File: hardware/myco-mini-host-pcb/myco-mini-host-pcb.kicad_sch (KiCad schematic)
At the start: 22 parts, among them J1 Conn_01x17_Female, J2 Conn_01x17_Female, Q1 AO3401A, Q2 AO3401A, SW1 EM-04-Q, U1 XC9145B33C0R-G, U2 SHT40-AD1B-R2, U3 BH1750FVI-TR

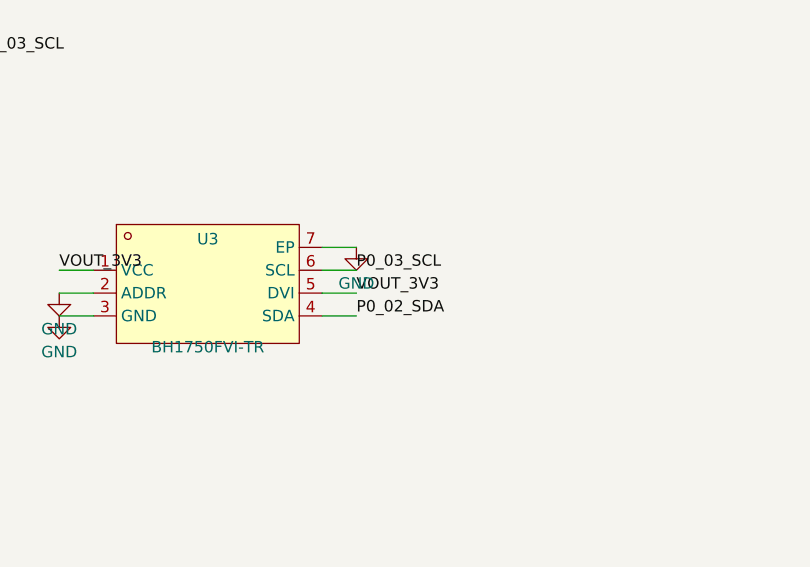
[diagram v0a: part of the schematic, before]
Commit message: fix: DVI du BH1750 sur VDD_NRF au lieu de VOUT_3V3 (cohérence avec les pull-ups I2C)
Le datasheet ROHM BH1750FVI définit VIH1 = 0.7 x DVI comme seuil logique haut
sur SDA/SCL. DVI était câblée sur VOUT_3V3 (3.3V fixe) alors que les pull-ups
I2C (R1/R2) sont sur VDD_NRF (~3.0V CR2032, peut descendre vers ~2.0V en fin
de vie de pile) — le seuil (2.31V) pouvait dépasser la tension réelle du bus
en fin de vie de pile, empêchant le BH1750 de reconnaître un "haut" valide.
DVI câblée maintenant sur le même rail que les pull-ups pour que le seuil
suive la tension réelle du bus. Point de séquencement DVI/VCC résiduel
documenté dans docs/pcb-design-decisions.md (non tranché, à valider en test).

Co-Authored-By: Claude Sonnet 5 <noreply@anthropic.com>
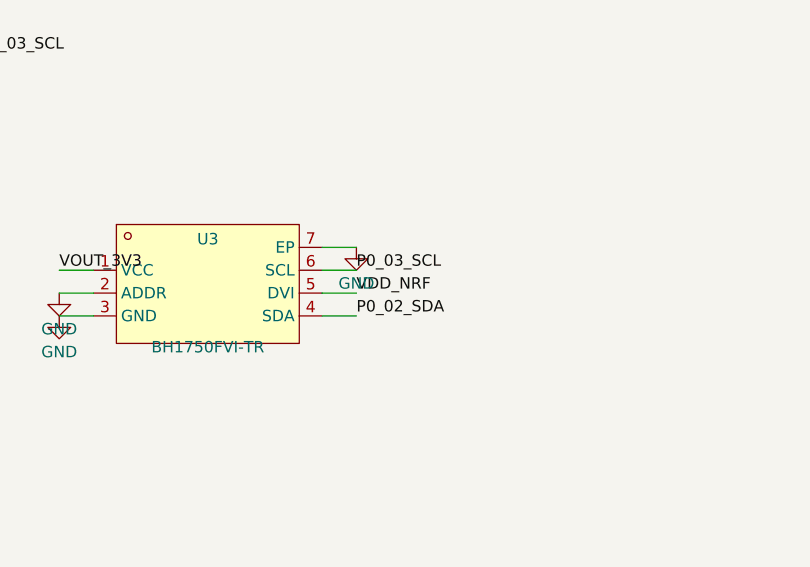
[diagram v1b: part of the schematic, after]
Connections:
- net VDD_NRF: now also U3.5 (DVI)
- net VOUT_3V3: no longer U3.5 (DVI)
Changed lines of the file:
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@@
     (effects (font (size 1.27 1.27)) (justify left bottom))
   )
-  (label "VOUT_3V3"
+  (label "VDD_NRF"
     (at 191.77 134.62 0)
     (effects (font (size 1.27 1.27)) (justify left bottom))

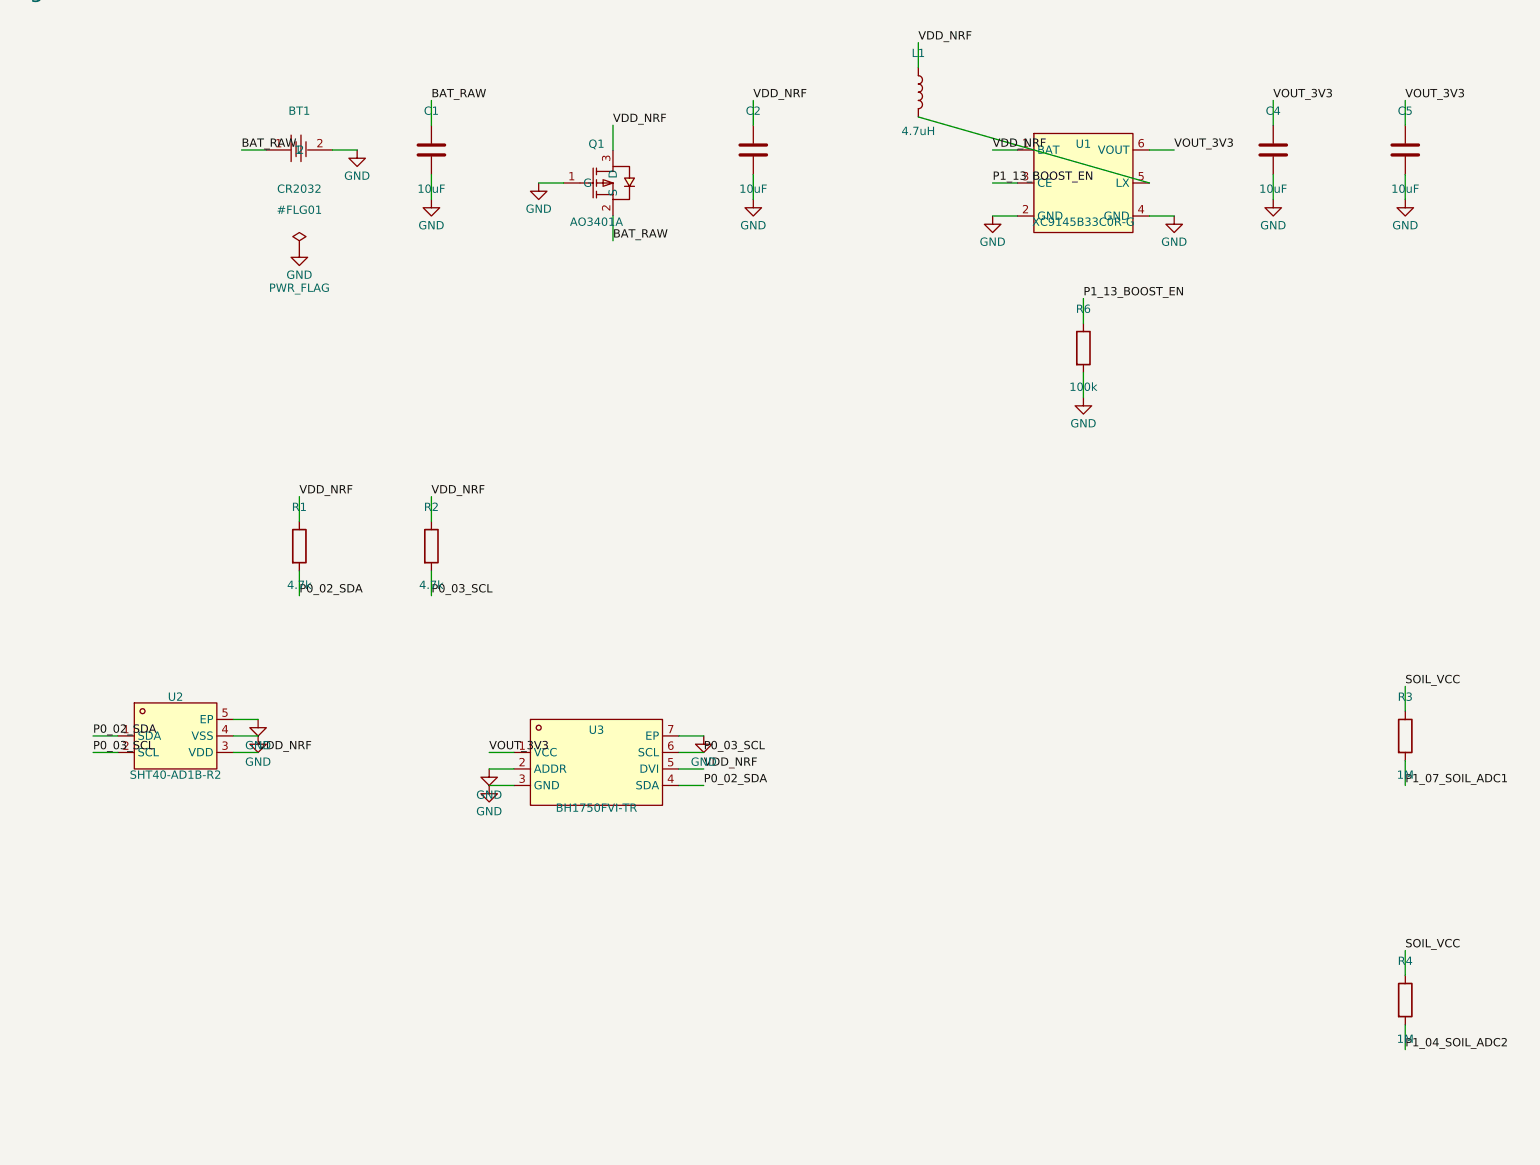
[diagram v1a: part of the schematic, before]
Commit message: fix: resolution XC9145 SOT-25, refonte sonde sol (profondeur), R3/R4 220k
- U1: XC9145B33C0R-G (WLP-6-05, non soudable a la main) -> XC9145B33CMR-G
  (SOT-25, LCSC C19261414, confirme en stock) - symbole/footprint refaits
- U2: SHT40 -> SHT41-AD1B-R2 (meme boitier/pinout, meilleure precision RH
  aux extremes)
- R3/R4: 1M -> 220k (1M hors plage source resistance max du SAADC nRF54L15,
  cf datasheet sec 11.17)
- Sonde sol: 36mm -> 60mm, doigts tournes a 90 (spines gauche/droite au
  lieu de haut/bas, moins fragiles mecaniquement), pitch 0.45mm -> 1.5mm
  et largeur 10mm -> 18mm pour la profondeur de penetration du champ dans
  le sol (~0.3mm -> ~1mm), compense par plus de doigts pour garder la
  capacite
- gen_pcb.py: PLACEMENT capture depuis le placement manuel valide (lecture
  seule du board actuel, pas de regeneration destructive)
- docs/pcb-design-decisions.md: sections 2.6/2.7/2.9/3.2 mises a jour avec
  le detail des calculs et sources
- misc/: ajout datasheet WLP-6-05 et reference Torex SOT-25 eval board

Co-Authored-By: Claude Sonnet 5 <noreply@anthropic.com>
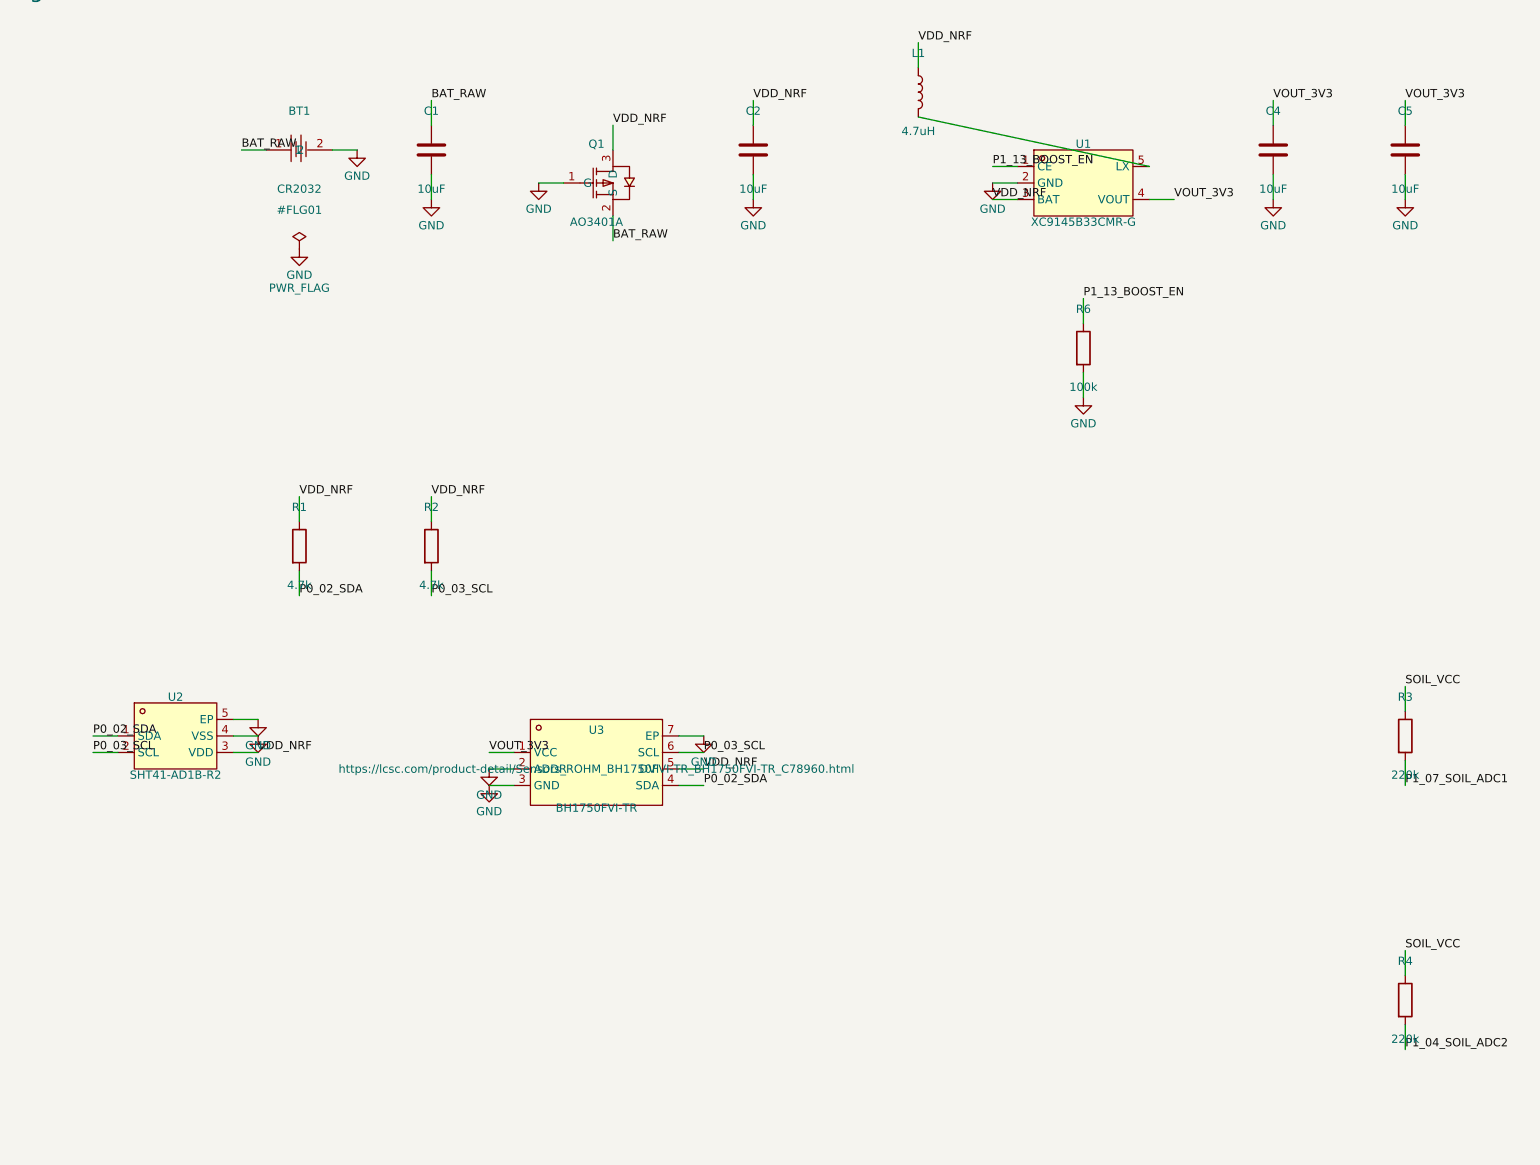
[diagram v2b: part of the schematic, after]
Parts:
- removed U1: XC9145B33C0R-G, myco_host:USON-6_XC9145_PLACEHOLDER, symbol myco_host:XC9145B33C0R-G
- removed U2: SHT40-AD1B-R2, myco_host:DFN-4_L1.5-W1.5-P0.8-TL-EP, symbol myco_host:SHT40-AD1B-R2
- added U1: XC9145B33CMR-G, myco_host:SOT-25-5_L2.9-W1.6-P0.95-LS2.8-BR, symbol myco_host:XC9145B33CMR-G
- added U2: SHT41-AD1B-R2, myco_host:DFN-4_L1.5-W1.5-P0.8-TL-EP, symbol myco_host:SHT41-AD1B-R2
- PROBE1: NOTE (none) -> PCB copper only, no purchased part. 2 interdigitated comb s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
- R3: value 1M -> 220k; Note Bias resistor, segment 1 (RC divider assumption - see decis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 -> Bias resistor, segment 1 - lowered from 1M, see decision lo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
- R4: value 1M -> 220k; Note Bias resistor, segment 2 (RC divider assumption - see decis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 -> Bias resistor, segment 2 - lowered from 1M, see decision lo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
- U3: LCSC Part (none) -> C78960
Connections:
- net GND: now also U1.2 (GND), U2.4 (VSS), U2.5 (EP)
- net P0_02_SDA: now also U2.1 (SDA)
- net P0_03_SCL: now also U2.2 (SCL)
- net P1_13_BOOST_EN: now also U1.1 (CE)
- net VDD_NRF: now also U1.3 (BAT), U2.3 (VDD)
- net VOUT_3V3: now also U1.4 (VOUT)
- net at L1.2: now also U1.5 (LX)

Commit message: feat: LED RGB feedback, decoupe thermique SHT41, contour symetrise, C6
Travail manuel de l'utilisateur dans l'éditeur KiCad (schéma + PCB),
documenté en détail dans docs/pcb-design-decisions.md (§2.10, §2.11) :

- LED RGB de feedback (D1, XL-5050RGBC) sur VOUT_3V3 — pinout corrigé
  après fourniture de la vraie datasheet Xinglight (3 LED indépendantes,
  pas anode commune ; l'hypothèse initiale inversait anode/cathode sur
  2 broches). Symbole/footprint refaits, câblage schéma corrigé
  chirurgicalement (add_rgb_led.py).
- Découpe thermique (3 fentes fermées) autour de U2 (SHT41), justifiée
  par le guide Sensirion (conduction thermique via PCB = source
  dominante d'erreur RH). Règle DRU mise à jour pour exclure U2 de la
  règle courtyard-to-edge.
- Contour de carte symétrisé par rapport à l'axe J1/J2 (X=77.75mm),
  recalculé par palier à partir des bounding boxes réelles des
  composants (premier essai par simple moyenne avait rogné dans U3/D1/
  R7-R9).
- C6 (100uF, decouplage) ajouté — cf. github issue #18.
- VDD SHT41/DVI BH1750 déjà déplacés vers VOUT_3V3 dans une session
  precedente (§2.5ter/§2.5quater), documentation mise à jour ici.

Aucune régénération gen_pcb.py/gen_schematic.py — édition manuelle
directe préservée (cf. mémoire feedback_pcb_placement).

Co-Authored-By: Claude Sonnet 5 <noreply@anthropic.com>
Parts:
- added C6: 100uF, Capacitor_SMD:C_0805_2012Metric, symbol Device:C
- added D1: LED_RGB_5050_CA, myco_host:LED_SMD5050-6P, symbol myco_host:LED_RGB_5050_CA
- added R7: 220, Resistor_SMD:R_0603_1608Metric, symbol Device:R
- added R8, R9: 330, Resistor_SMD:R_0603_1608Metric, symbol Device:R
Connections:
- net GND: now also C6.2
- net P0_02_SDA: no longer R1.2, U2.1 (SDA), U3.4 (SDA)
- net P0_03_SCL: no longer R2.2, U2.2 (SCL), U3.6 (SCL)
- net VDD_NRF: now also C6.1; no longer R1.1, R2.1, U2.3 (VDD), U3.5 (DVI)
- net VOUT_3V3: now also R1.1, R2.1, U2.3 (VDD), U3.5 (DVI), D1.4 (A), D1.5 (A), D1.6 (A)
- net P2_06_LED_B: now reaches J2.11 (Pin_11)
- net P2_06_LED_B: now also R9.2
- net P2_05_LED_G: now reaches J2.12 (Pin_12)
- net P2_05_LED_G: now also R7.2
- net P2_04_LED_R: now reaches J2.13 (Pin_13)
- net P2_04_LED_R: now also R8.2
- net P1_10_SDA: now reaches J1.3 (Pin_3)
- net P1_10_SDA: now also R1.2, U2.1 (SDA), U3.6 (SCL)
- net P1_11_SCL: now reaches J1.4 (Pin_4)
- net P1_11_SCL: now also R2.2, U2.2 (SCL), U3.4 (SDA)
- new net LED_B_NODE: D1.1 (B), R9.1
- new net LED_G_NODE: D1.3 (G), R8.1
- new net LED_R_NODE: D1.2 (R), R7.1

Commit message: feat: protection backfeed (U4/MAX40203), rail nRF54 sur boost, remap GPIO
- U4 (MAX40203AUK+T): diode ideale entre Q1 et VDD_NRF, bloque le
  backfeed depuis le probe SWD (breakout J5) vers la CR2032 - remplace
  la premiere tentative LM66100 (rejetee apres verification, seuil
  RCB trop insensible pour nos courants)
- SW1: EM-04-Q remplace par DM-04-V (rupture de stock LCSC), meme
  pairing electrique, footprint tourne 90deg
- Bouton reset SW2 (TS-1187A-B-A-B) + R10 series sur NRESET (J2 pin1)
- Fix SDA/SCL inverses sur U3 (BH1750) - bug trouve par audit, U3.4
  et U3.6 etaient sur les mauvais nets
- Architecture alim revue : le nRF54 (J1 pin9) passe de VDD_NRF (pile
  directe) a VOUT_3V3 (boost, toujours actif) pour eliminer le
  depassement d'abs-max GPIO (VDD+0.3V) cause par les pull-ups
  VOUT_3V3 sur des pins references a VDD_NRF qui sague avec la pile
  - Q3 (AO3401A) : nouveau switch VOUT_3V3->SENSOR_3V3, alimente
    SHT41+BH1750+leurs pull-ups I2C (R1/R2), coupable independamment
  - Q4 (AO3401A) + R11/R12 (diviseur 1M/1M) : mesure batterie via
    BAT_RAW, switchee pour eviter la fuite continue (remplace le
    canal SAADC interne VDD, plus valide une fois VDD_NRF regule)
  - Q3/Q4 partagent un seul GPIO de controle (P1_12_SENSOR_EN)
- Remap GPIO pour faciliter le routage : BOOST_EN P1.13->P1.05,
  BAT_SENSE P1.05->P1.13, SOIL_SW P1.14->P1.08 (tous verifies
  General Purpose I/O dans la datasheet nRF54L15, P1.13 confirme
  AIN6 pour le besoin SAADC de BAT_SENSE)
- BOM et librairie (symboles/footprints/modeles 3D) mis a jour

Co-Authored-By: Claude Sonnet 5 <noreply@anthropic.com>
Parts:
- added Q3, Q4: AO3401A, myco_host:SOT-23_L2.9-W1.3-P1.90-LS2.4-BR, symbol myco_host:AO3401A
- added R10: 220, Resistor_SMD:R_0603_1608Metric, symbol Device:R
- added R11, R12: 1M, Resistor_SMD:R_0603_1608Metric, symbol Device:R
- added SW2: TS-1187A-B-A-B, myco_host:SW-SMD_4P-L5.1-W5.1-P3.70-LS6.5-TL_H1.5, symbol myco_host:TS-1187A-B-A-B
- added U4: MAX40203AUK+T, myco_host:SOT-23-5_L3.0-W1.6-P0.95-LS2.8-BR, symbol myco_host:MAX40203AUK+T
- Q1: Note Reverse polarity protect: S=BAT_RAW D=VDD_NRF G=GND -> Reverse polarity protect ONLY: S=BAT_RAW D=VDD_PROT G=GND. 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
- SW1: value EM-04-Q -> DM-04-V; footprint myco_host:SW-SMD_8P-L10.1-W6.0-P2.54-LS9.8 -> myco_host:SW-SMD_8P-L11.1-W6.2-P2.54-LS9.8; symbol myco_host:EM-04-Q_C501635 -> myco_host:DM-04-V; LCSC C501635 -> C501537; Note Pin pairing 1-8,2-7,3-6,4-5 verified from EasyEDA symbol ge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 -> Swapped from EM-04-Q (out of stock at LCSC as of 2026-08-22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
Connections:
- net BAT_RAW: now also Q4.2 (S)
- net GND: now also R12.2, SW2.3 (C), U4.2 (GND)
- net P1_10_SDA: now also U3.4 (SDA); no longer U3.6 (SCL)
- net P1_11_SCL: now also U3.6 (SCL); no longer U3.4 (SDA)
- net VDD_NRF: now also U4.5 (OUT); no longer C3.1, C6.1, J1.9 (Pin_9), Q1.3 (D)
- net VOUT_3V3: now also C3.1, C6.1, J1.9 (Pin_9), Q3.2 (S); no longer R1.1, R2.1, U2.3 (VDD), U3.1 (VCC), U3.5 (DVI)
- net NRESET: now reaches J2.1 (Pin_1)
- net NRESET: now also R10.1
- net P1_05_BOOST_EN: now reaches J1.13 (Pin_13)
- net P1_05_BOOST_EN: now also R6.1, U1.1 (CE)
- net P1_08_SOIL_SW: now reaches J1.16 (Pin_16)
- net P1_08_SOIL_SW: now also Q2.1 (G), R5.2
- net P1_12_SENSOR_EN: now reaches J1.5 (Pin_5)
- net P1_12_SENSOR_EN: now also Q3.1 (G), Q4.1 (G)
- removed net P1_13_BOOST_EN: J1.6 (Pin_6), R6.1, U1.1 (CE)
- removed net P1_14_SOIL_SW: J1.7 (Pin_7), Q2.1 (G), R5.2
- new net: R10.2, SW2.1 (A)
- new net BAT_SENSE_TOP: Q4.3 (D), R11.1
- new net P1_13_BAT_SENSE: J1.6 (Pin_6), R11.2, R12.1
- new net SENSOR_3V3: Q3.3 (D), R1.1, R2.1, U2.3 (VDD), U3.1 (VCC), U3.5 (DVI)
- new net VDD_PROT: Q1.3 (D), U4.1 (VDD), U4.3 (EN)
